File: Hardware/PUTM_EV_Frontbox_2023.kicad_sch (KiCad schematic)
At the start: 24 parts, among them J1 Conn_02x16_Counter_Clockwise, J2 Conn_01x10_Pin, U1 LM4040C33FTA, U2 STM32G473RCTx

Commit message: Changes in current layout, added tensometers to layout
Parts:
- removed J2: Conn_01x10_Pin, symbol Connector:Conn_01x10_Pin
- added J3, J4: M80-5100622, Snapeda:M80-5100622_HARWIN_M80-5100622, symbol Snapeda:M80-5100622
- J1: footprint Connector_IDC:IDC-Header_2x17_P2.54mm_Vertical -> Connector_IDC:IDC-Header_2x17-1MP_P2.54mm_Latch6.5mm_Vertical
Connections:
- net GND: now also J3.6, J4.1
- net Tensometers/OUT1+: now also J4.3
- net Tensometers/OUT1-: now also J4.4
- net Tensometers/OUT2+: now also J4.5
- net Tensometers/OUT2-: now also J4.6
- net Tensometers/OUT3+: now also J3.1
- net Tensometers/OUT3-: now also J3.2
- net Tensometers/OUT4+: now also J3.3
- net Tensometers/OUT4-: now also J3.4
- net Tensometer_1 renamed Tensometer 1
- net Tensometer_2 renamed Tensometer 2
- net Tensometer_3 renamed Tensometer 3
- net Tensometer_4 renamed Tensometer 4
- new net Tensometers/12V1: J4.2
- new net Tensometers/12V2: J3.5
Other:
- removed sheet steering_position
- added sheet Steering_Position (Steering_position.kicad_sch)
- sheet Tensometers: file untitled.kicad_sch -> Tensometers.kicad_sch
- sheet Tensometers ports: added 12V1, 12V2; removed 12V
- note added: "Oscillator"
- note added: "Tensometers"
- moved on the sheet: D1, D2, D3, D4, H1, H2, H3, H4, R101, R102, R5, R6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

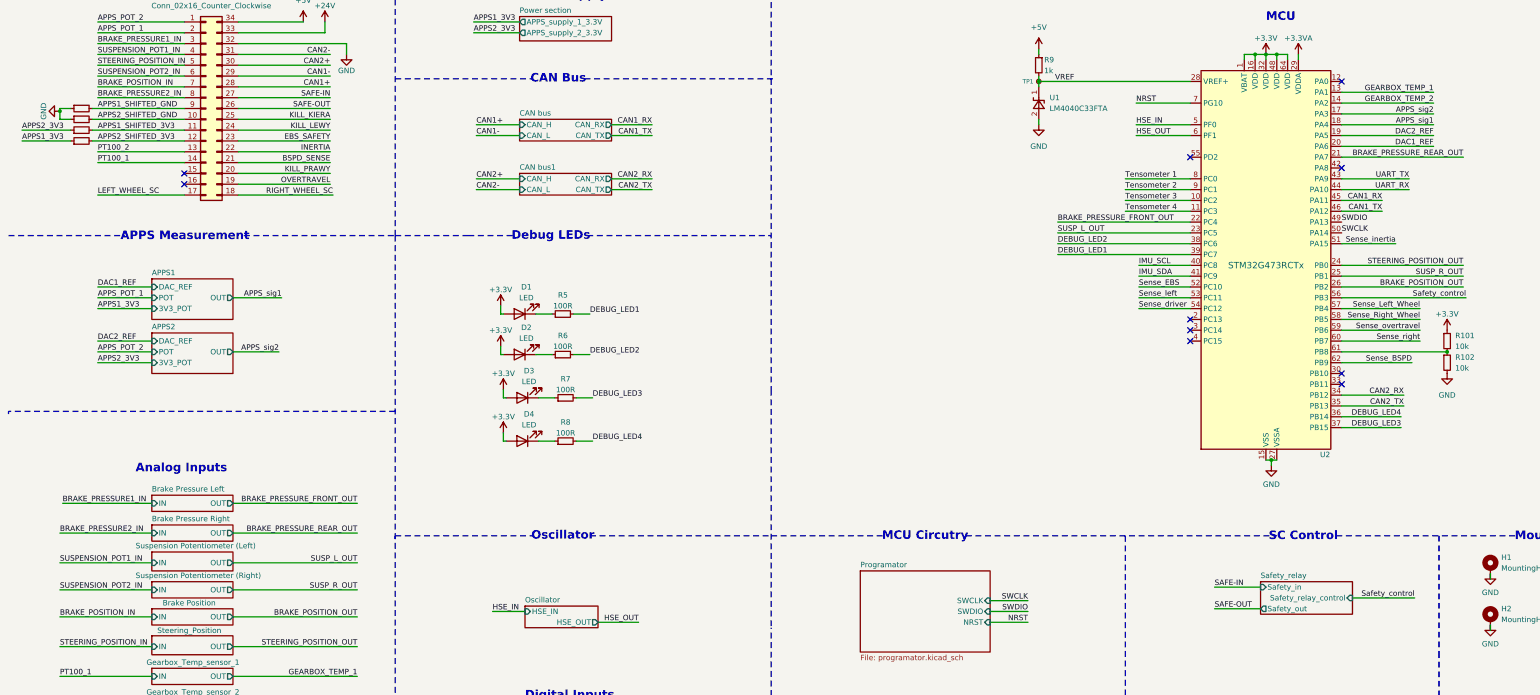
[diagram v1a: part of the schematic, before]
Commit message: Changes for new steering position system
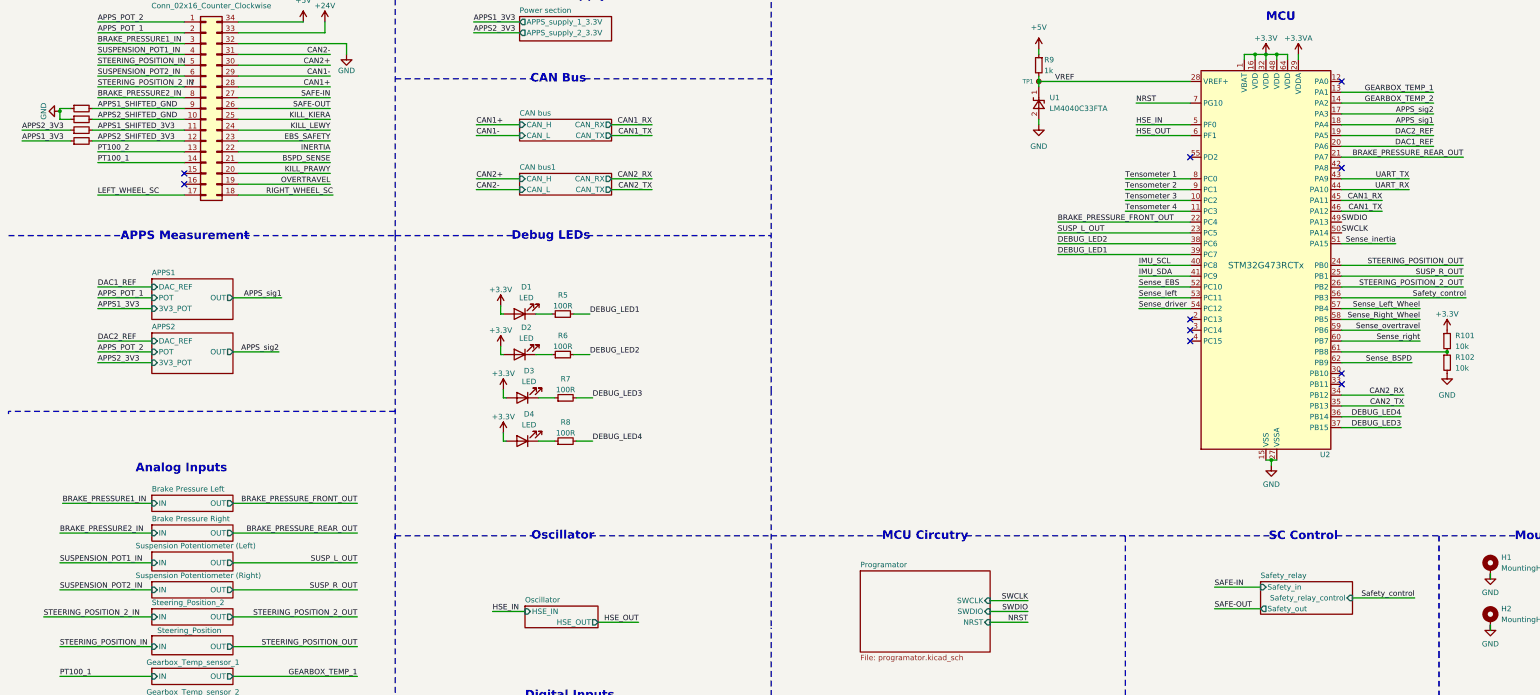
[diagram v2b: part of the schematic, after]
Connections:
- net BRAKE_POSITION_IN renamed STEERING_POSITION_2_IN
- net BRAKE_POSITION_OUT renamed STEERING_POSITION_2_OUT
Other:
- removed sheet Brake Position
- added sheet Steering_Position_2 (Steering_Position_2.kicad_sch)
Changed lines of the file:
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@@
 	(wire
 		(pts
-			(xy 24.13 163.83) (xy 45.72 163.83)
+			(xy 20.32 163.83) (xy 45.72 163.83)
 		)
 		(stroke
@@
 		)
 	)
-	(label "BRAKE_POSITION_IN"
-		(at 24.13 163.83 0)
+	(label "STEERING_POSITION_2_IN"
+		(at 20.32 163.83 0)
 		(fields_autoplaced yes)
 		(effects
@@
 		)
 	)
-	(label "BRAKE_POSITION_OUT"
+	(label "STEERING_POSITION_2_OUT"
 		(at 353.695 86.36 180)
 		(fields_autoplaced yes)
@@
 		)
 	)
-	(label "BRAKE_POSITION_OUT"
+	(label "STEERING_POSITION_2_OUT"
 		(at 93.98 163.83 180)
 		(fields_autoplaced yes)
@@
 		)
 	)
-	(label "BRAKE_POSITION_IN"
+	(label "STEERING_POSITION_2_IN"
 		(at 33.02 39.37 0)
 		(fields_autoplaced yes)
@@
 	)
 	(sheet
+		(at 45.72 161.925)
+		(size 19.05 3.81)
+		(fields_autoplaced yes)
+		(stroke
+			(width 0.1524)
+			(type solid)
+		)
+		(fill
+			(color 0 0 0 0.0000)
+		)
+		(property "Sheetname" "Steering_Position_2"
+			(at 45.72 161.2134 0)
+			(effects
+				(font
+					(size 1.27 1.27)
+				)
+				(justify left bottom)
+			)
+		)
+		(property "Sheetfile" "Steering_Position_2.kicad_sch"
+			(at 45.72 166.3196 0)
+			(effects
+				(font
+					(size 1.27 1.27)
+				)
+				(justify left top)
+				(hide yes)
+			)
+		)
+		(pin "IN" input
+			(at 45.72 163.83 180)
+			(effects
+				(font
+					(size 1.27 1.27)
+				)
+				(justify left)
+			)
+		)
+		(pin "OUT" output
+			(at 64.77 163.83 0)
+			(effects
+				(font
+					(size 1.27 1.27)
+				)
+				(justify right)
+			)
+		)
+		(instances
+			(project "PUTM_EV_Frontbox_2023"
+				(path "/b652b05a-4e3d-4ad1-b032-18886abe7d45"
+					(page "20")
+				)
+			)
+		)
+	)
+	(sheet
 		(at 132.08 46.99)
 		(size 21.59 5.08)
@@
 				)
 			)
-		)
-	)
-	(sheet
-		(at 45.72 161.925)
-		(size 19.05 3.81)
-		(stroke
-			(width 0.1524)
-			(type solid)
-		)
-		(fill
-			(color 0 0 0 0.0000)
-		)
-		(property "Sheetname" "Brake Position"
-			(at 48.26 161.29 0)
-			(effects
-				(font
-					(size 1.27 1.27)
-				)
-				(justify left bottom)
-			)
-		)
-		(property "Sheetfile" "suspension_potentiometer.kicad_sch"
-			(at 38.735 176.53 0)
-			(effects
-				(font
-					(size 1.27 1.27)
-				)
-				(justify left top)
-				(hide yes)
-			)
-		)
-		(pin "IN" input
-			(at 45.72 163.83 180)
-			(effects
-				(font
-					(size 1.27 1.27)
-				)
-				(justify left)
-			)
-		)
-		(pin "OUT" output
-			(at 64.77 163.83 0)
-			(effects
-				(font
-					(size 1.27 1.27)
-				)
-				(justify right)
-			)
-		)
-		(instances
-			(project "PUTM_EV_Frontbox_2023"
-				(path "/b652b05a-4e3d-4ad1-b032-18886abe7d45"
-					(page "5")
-				)
-			)

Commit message: Changes in power section
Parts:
- TP1: footprint TestPoint:TestPoint_Pad_D1.0mm -> TestPoint:TestPoint_THTPad_D1.0mm_Drill0.5mm
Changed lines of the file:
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@@
 			)
 		)
-		(property "Footprint" "TestPoint:TestPoint_Pad_D1.0mm"
+		(property "Footprint" "TestPoint:TestPoint_THTPad_D1.0mm_Drill0.5mm"
 			(at 259.08 38.1 0)
 			(effects

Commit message: Frontbox 2025 Version 1.0
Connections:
- no-connect marks 10 -> 12

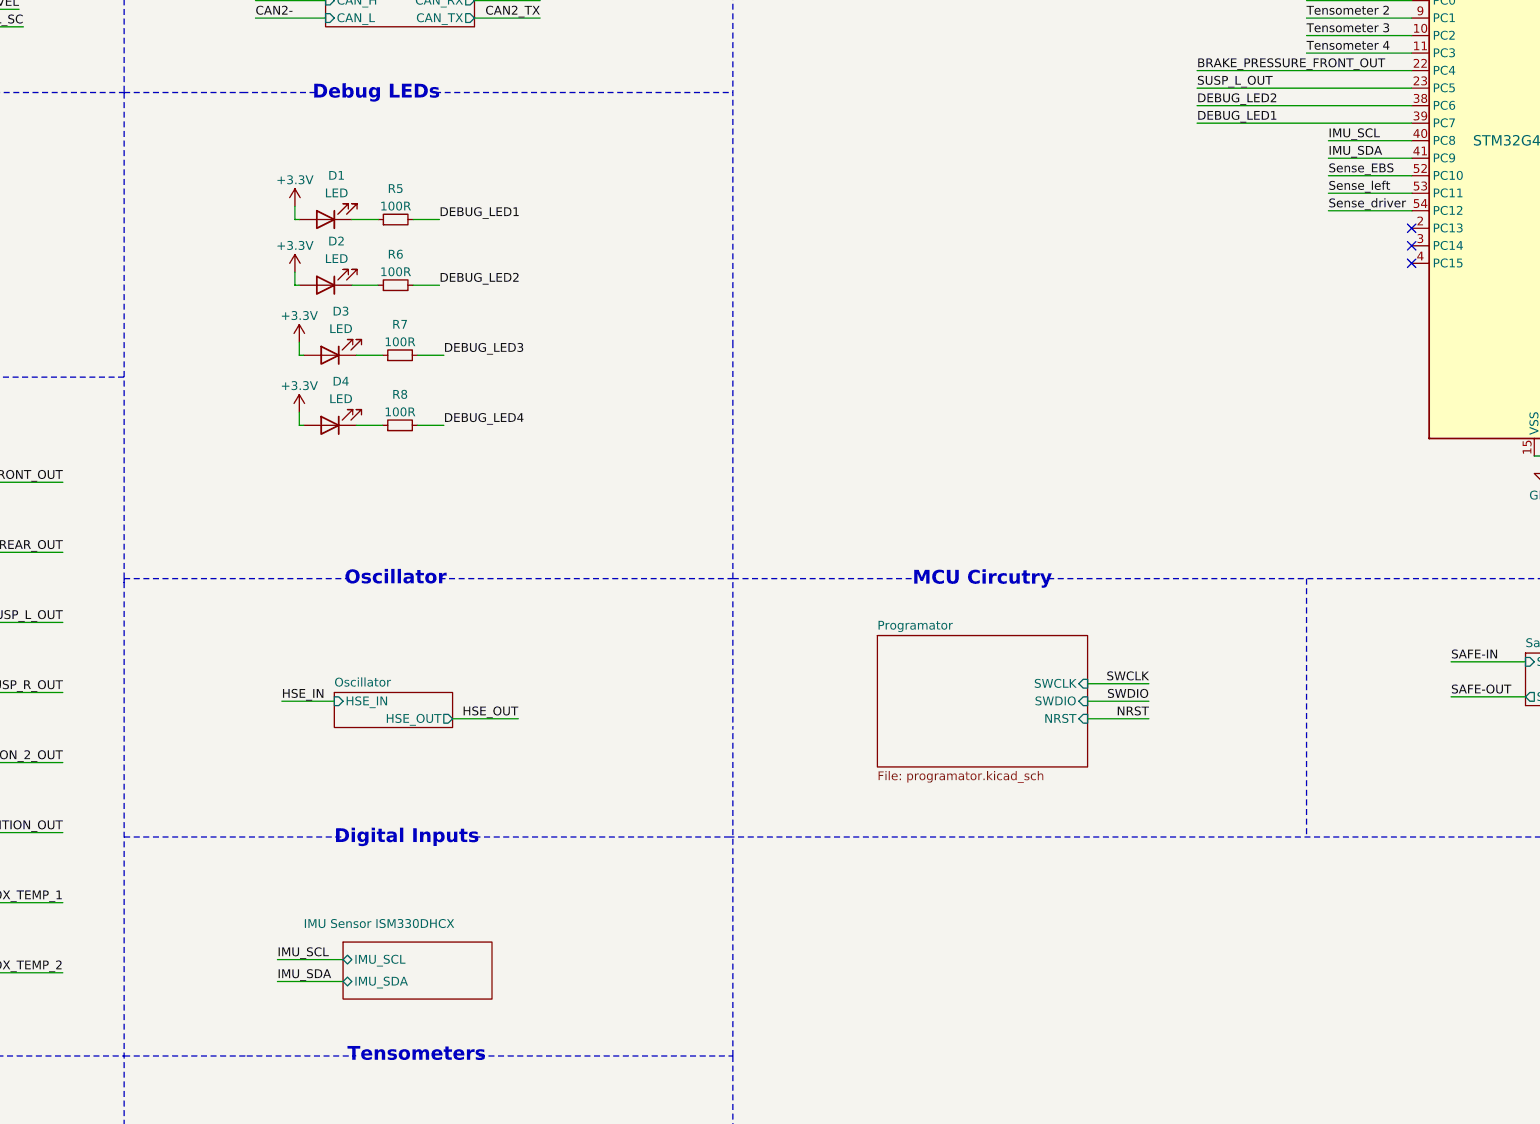
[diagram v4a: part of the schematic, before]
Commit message: Deleted IMU
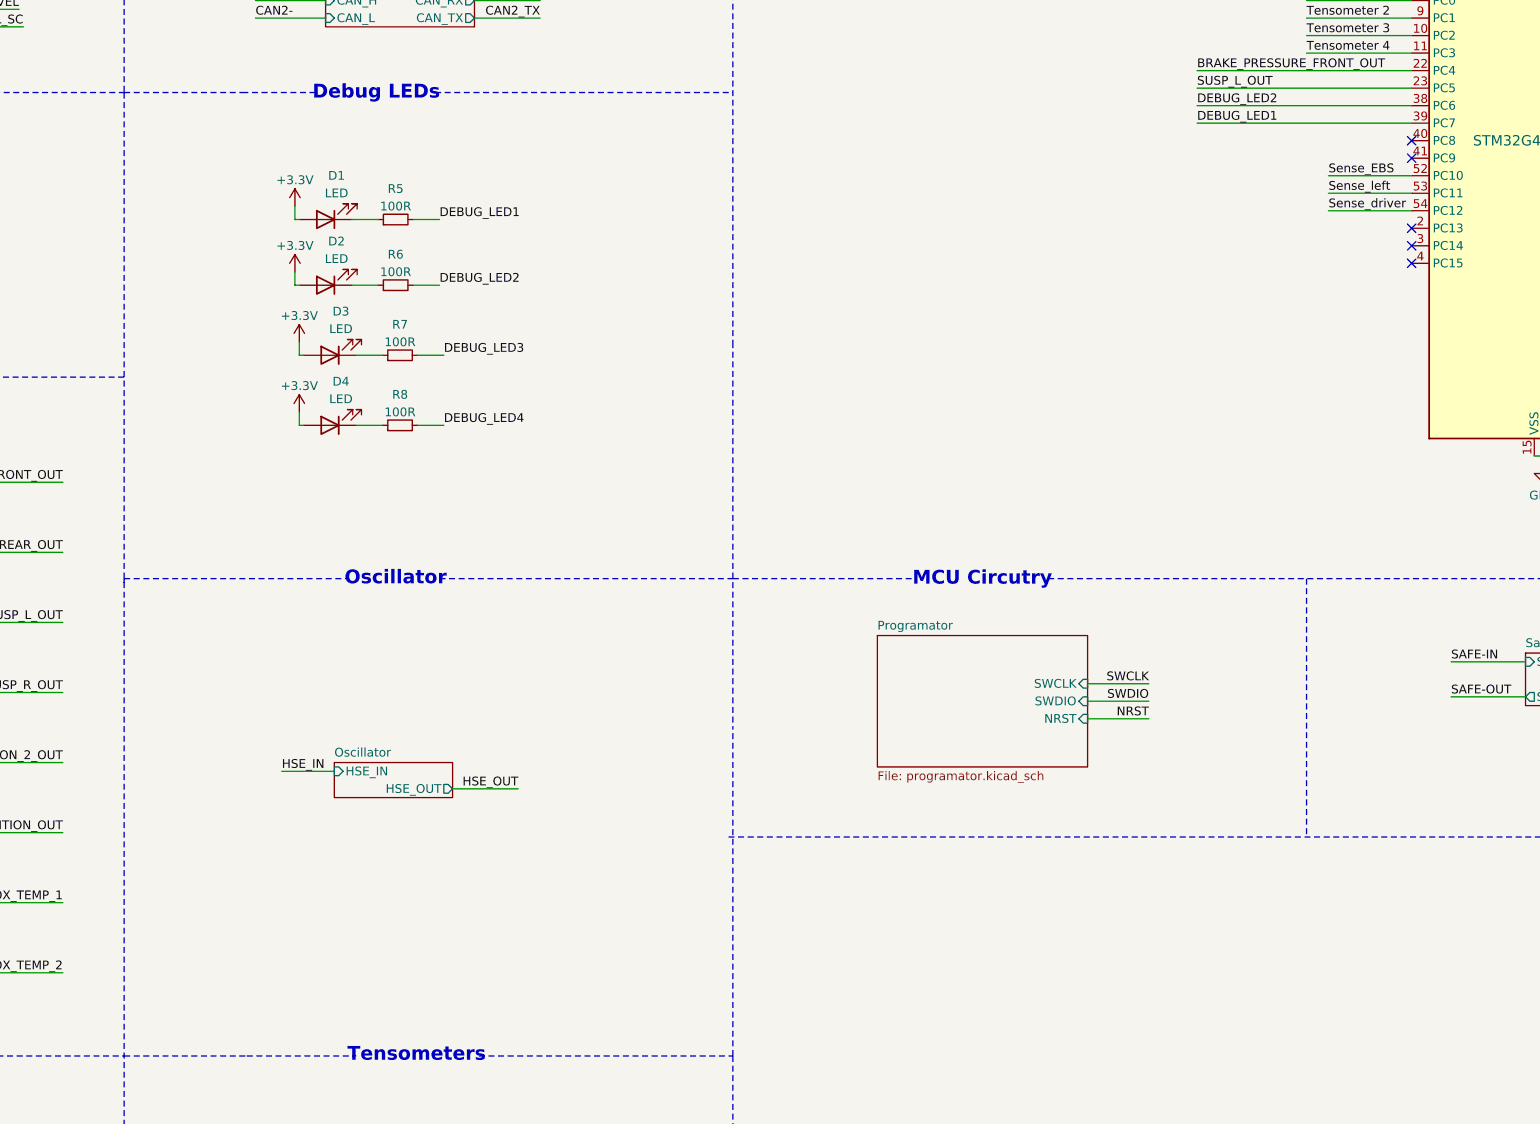
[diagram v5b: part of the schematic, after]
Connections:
- net IMU_SCL: no longer names the net of U2.40 (PC8)
- net IMU_SDA: no longer names the net of U2.41 (PC9)
- no-connect marks 12 -> 14
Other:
- removed sheet IMU Sensor ISM330DHCX
- note removed: "Digital Inputs"
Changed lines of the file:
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@@
 	)
 	(no_connect
+		(at 289.56 83.82)
+	)
+	(no_connect
 		(at 325.12 58.42)
 	)
@@
 		(at 53.34 59.69)
 	)
+	(no_connect
+		(at 289.56 81.28)
+	)
 	(polyline
 		(pts
@@
 	(wire
 		(pts
-			(xy 125.73 162.56) (xy 133.35 162.56)
+			(xy 125.73 172.72) (xy 133.35 172.72)
 		)
 		(stroke
@@
 	(wire
 		(pts
-			(xy 125.095 200.025) (xy 134.62 200.025)
-		)
-		(stroke
-			(width 0)
-			(type default)
-		)
-	)
-	(wire
-		(pts
 			(xy 325.12 116.84) (xy 339.09 116.84)
 		)
@@
 	(wire
 		(pts
-			(xy 150.495 165.1) (xy 160.02 165.1)
+			(xy 150.495 175.26) (xy 160.02 175.26)
 		)
 		(stroke
@@
 	(wire
 		(pts
-			(xy 277.495 81.28) (xy 289.56 81.28)
-		)
-		(stroke
-			(width 0)
-			(type default)
-		)
-	)
-	(wire
-		(pts
 			(xy 66.04 29.21) (xy 91.44 29.21)
 		)
@@
 	(wire
 		(pts
-			(xy 125.095 203.2) (xy 134.62 203.2)
-		)
-		(stroke
-			(width 0)
-			(type default)
-		)
-	)
-	(wire
-		(pts
 			(xy 74.93 243.84) (xy 76.835 243.84)
 		)
@@
 	(wire
 		(pts
-			(xy 277.495 83.82) (xy 289.56 83.82)
-		)
-		(stroke
-			(width 0)
-			(type default)
-		)
-	)
-	(wire
-		(pts
 			(xy 383.54 153.67) (xy 383.54 154.94)
 		)
@@
 		)
 	)
-	(polyline
-		(pts
-			(xy 153.67 182.245) (xy 190.5 182.245)
-		)
-		(stroke
-			(width 0)
-			(type dot)
-		)
-	)
 	(wire
 		(pts
@@
 		)
 	)
-	(polyline
-		(pts
-			(xy 102.87 182.245) (xy 134.62 182.245)
-		)
-		(stroke
-			(width 0)
-			(type dot)
-		)
-	)
 	(wire
 		(pts
@@
 		)
 	)
-	(text "Digital Inputs\n\n"
-		(exclude_from_sim no)
-		(at 133.35 186.69 0)
-		(effects
-			(font
-				(size 2 2)
-				(thickness 0.4)
-				(bold yes)
-			)
-			(justify left bottom)
-		)
-	)
 	(text "Analog Inputs\n\n"
 		(exclude_from_sim no)
@@
 		)
 	)
-	(label "IMU_SDA"
-		(at 277.495 83.82 0)
-		(fields_autoplaced yes)
-		(effects
-			(font
-				(size 1.27 1.27)
-			)
-			(justify left bottom)
-		)
-	)
 	(label "Tensometer 3"
 		(at 274.32 66.04 0)
@@
 	)
 	(label "HSE_IN"
-		(at 125.73 162.56 0)
+		(at 125.73 172.72 0)
 		(fields_autoplaced yes)
 		(effects
@@
 		)
 	)
-	(label "IMU_SDA"
-		(at 125.095 203.2 0)
-		(fields_autoplaced yes)
-		(effects
-			(font
-				(size 1.27 1.27)
-			)
-			(justify left bottom)
-		)
-	)
 	(label "Sense_left"
 		(at 76.835 236.22 0)
@@
 	)
 	(label "HSE_OUT"
-		(at 160.02 165.1 180)
+		(at 160.02 175.26 180)
 		(fields_autoplaced yes)
 		(effects
@@
 		)
 	)
-	(label "IMU_SCL"
-		(at 277.495 81.28 0)
-		(fields_autoplaced yes)
-		(effects
-			(font
-				(size 1.27 1.27)
-			)
-			(justify left bottom)
-		)
-	)
 	(label "Sense_BSPD"
 		(at 341.63 104.14 180)
@@
 		)
 	)
-	(label "IMU_SCL"
-		(at 125.095 200.025 0)
-		(fields_autoplaced yes)
-		(effects
-			(font
-				(size 1.27 1.27)
-			)
-			(justify left bottom)
-		)
-	)
 	(label "SUSPENSION_POT2_IN"
 		(at 24.13 161.29 0)
@@
 	)
 	(sheet
-		(at 133.35 161.29)
+		(at 133.35 171.45)
 		(size 17.145 5.08)
 		(fields_autoplaced yes)
@@
 		)
 		(property "Sheetname" "Oscillator"
-			(at 133.35 160.5784 0)
+			(at 133.35 170.7384 0)
 			(effects
 				(font
@@
 		)
 		(property "Sheetfile" "oscillator.kicad_sch"
-			(at 133.35 166.9546 0)
+			(at 133.35 177.1146 0)
 			(effects
 				(font
@@
 		)
 		(pin "HSE_IN" input
-			(at 133.35 162.56 180)
+			(at 133.35 172.72 180)
 			(effects
 				(font
@@
 		)
 		(pin "HSE_OUT" output
-			(at 150.495 165.1 0)
+			(at 150.495 175.26 0)
 			(effects
 				(font
@@
 				)
 			)
-		)
-	)
-	(sheet
-		(at 134.62 197.485)
-		(size 21.59 8.255)
-		(stroke
-			(width 0.1524)
-			(type solid)
-		)
-		(fill
-			(color 0 0 0 0.0000)
-		)
-		(property "Sheetname" "IMU Sensor ISM330DHCX"
-			(at 128.905 195.58 0)
-			(effects
-				(font
-					(size 1.27 1.27)
-				)
-				(justify left bottom)
-			)
-		)
-		(property "Sheetfile" "imu_sensor.kicad_sch"
-			(at 133.35 206.375 0)
-			(effects
-				(font
-					(size 1.27 1.27)
-				)
-				(justify left top)
-				(hide yes)
-			)
-		)
-		(pin "IMU_SCL" bidirectional
-			(at 134.62 200.025 180)
-			(effects
-				(font
-					(size 1.27 1.27)
-				)
-				(justify left)
-			)
-		)
-		(pin "IMU_SDA" bidirectional
-			(at 134.62 203.2 180)
-			(effects
-				(font
-					(size 1.27 1.27)
-				)
-				(justify left)
-			)
-		)
-		(instances
-			(project "PUTM_EV_Frontbox_2023"
-				(path "/b652b05a-4e3d-4ad1-b032-18886abe7d45"
-					(page "2")
-				)
-			)
